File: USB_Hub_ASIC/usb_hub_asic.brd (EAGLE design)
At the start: 101.6 x 76.2 mm, 105 parts, among them J1 CONN_RCPT_USB3.0_TYPEB_9POS_R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, J2 CONN_RCPT_USB3.0_TYPEA_9POS_R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, J3 CONN_RCPT_USB3.0_TYPEA_9POS_R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, J4 CONN_RCPT_USB3.0_TYPEA_9POS_R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, J5 CONN_RCPT_USB3.0_TYPEA_9POS_R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, Q1 26M, U1 IC_MCP1603LT-330_3.3V_500MA_B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, U2 IC_CYUSB3314_QUAD_USB3.0_HUB, U3 IC_LM3674MF-1.2/NOPB_1.2V_600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

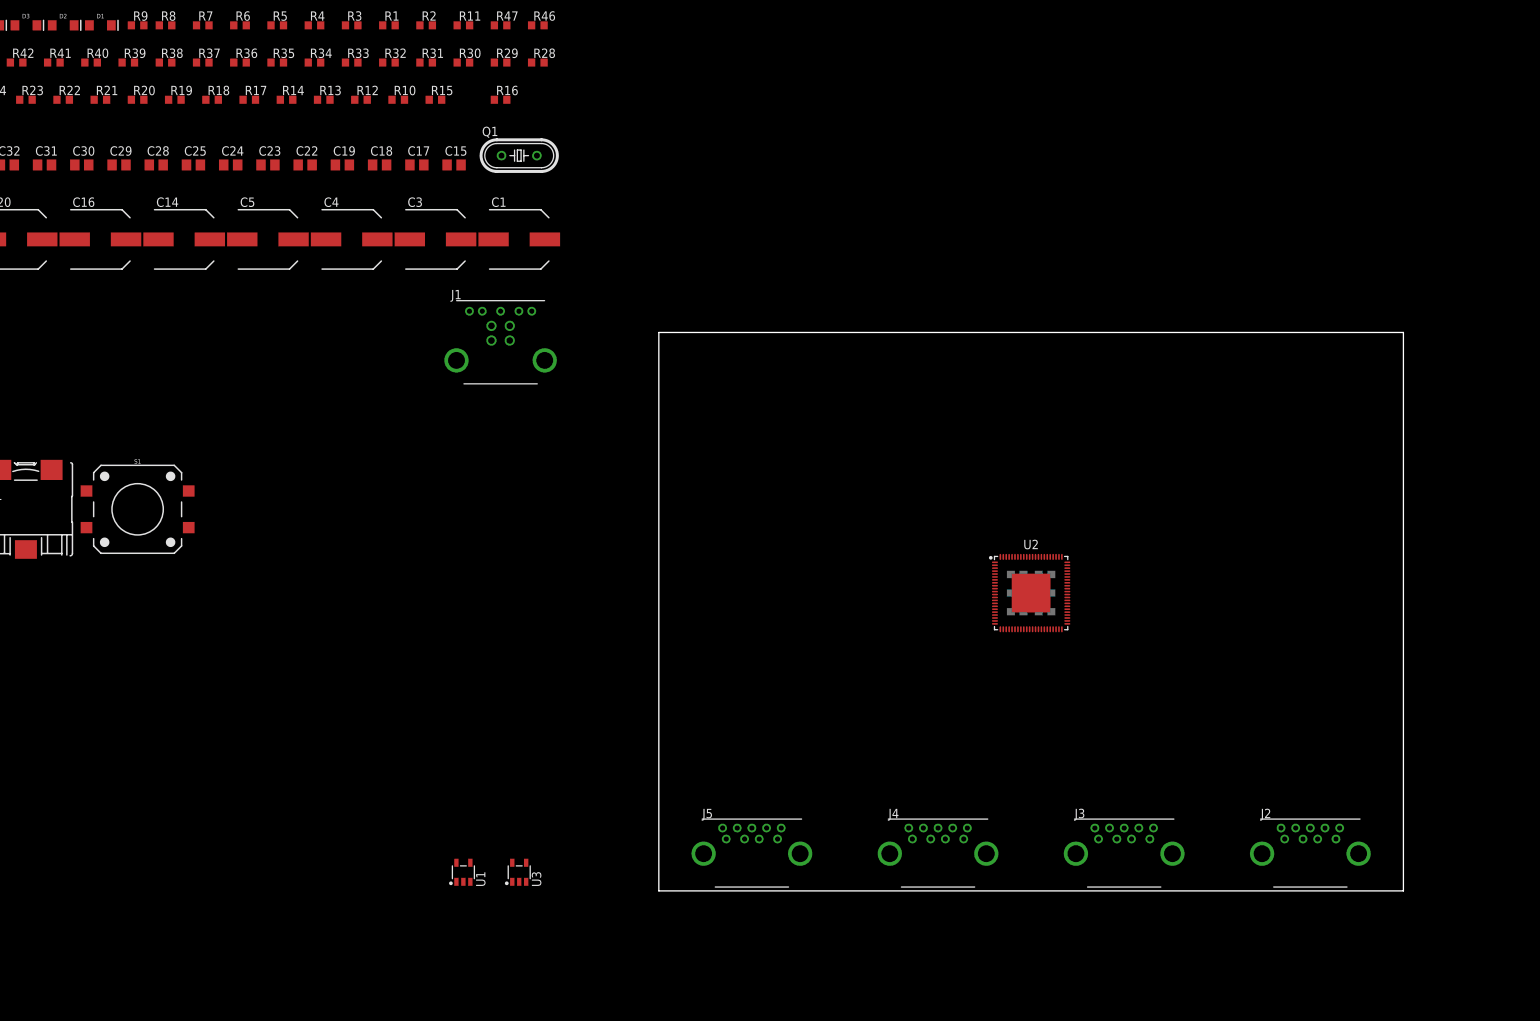
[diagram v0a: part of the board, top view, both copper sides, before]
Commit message: Power plane routing for chip
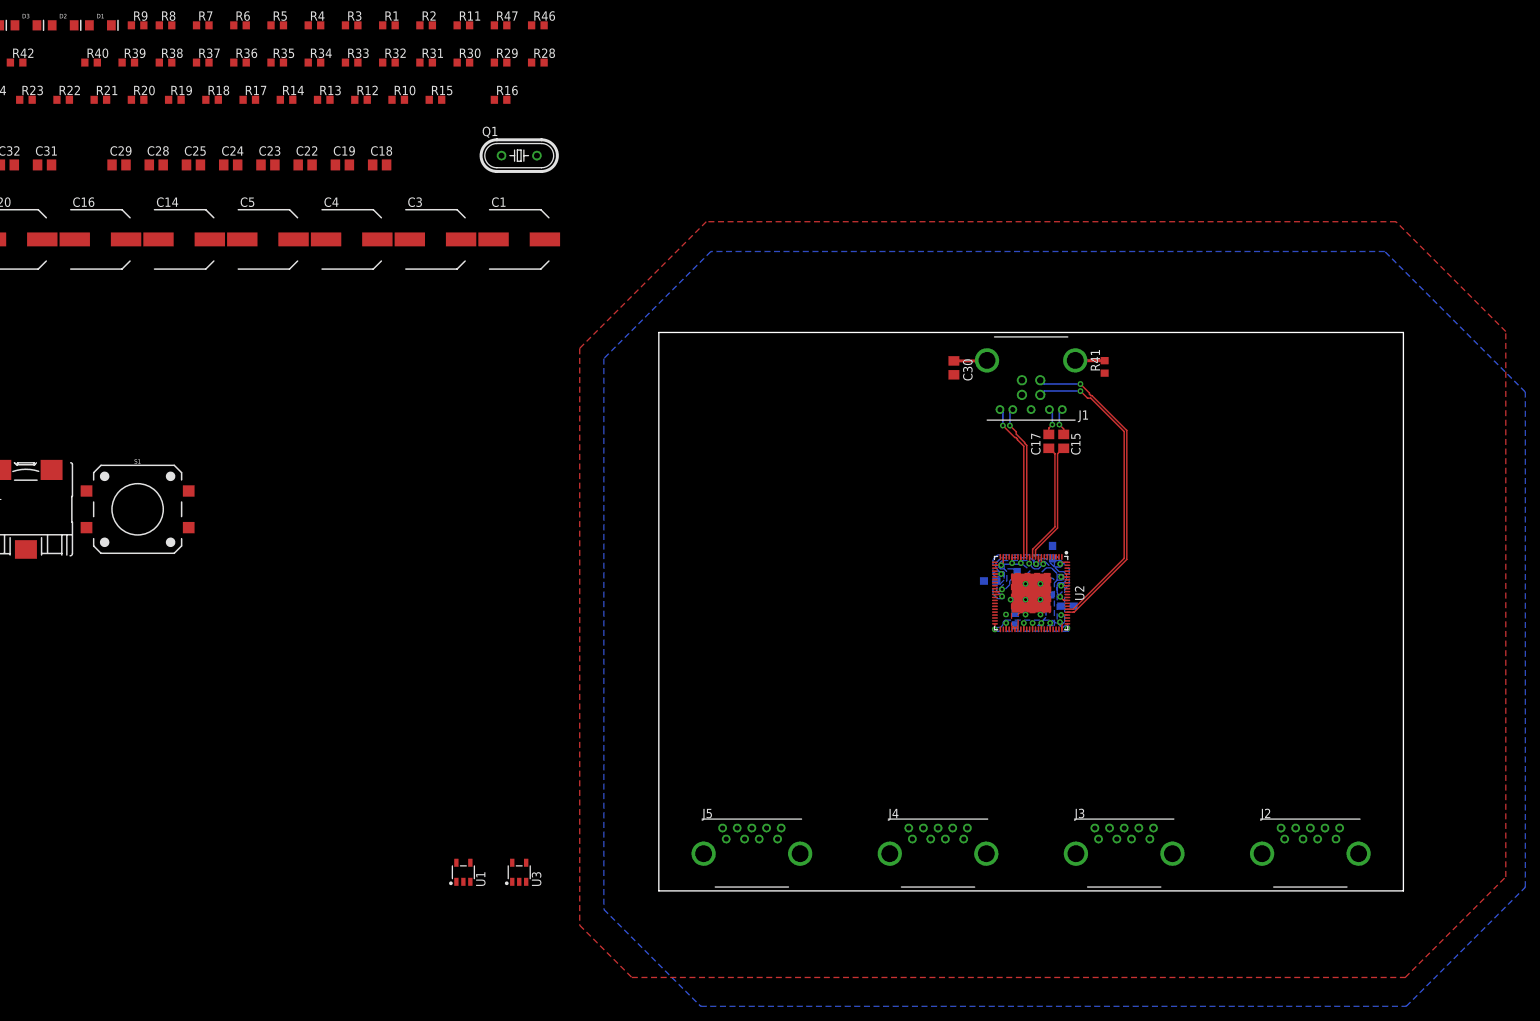
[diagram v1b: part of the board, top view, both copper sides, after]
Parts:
- moved R41 149.3 mm to (60.8, 71.5), turned to 90 degrees
- moved C30 122.2 mm to (40.3, 71.4), turned to 270 degrees
- moved C17 94.1 mm to (53.2, 61.3), turned to 90 degrees
- moved C15 91.3 mm to (55.2, 61.3), turned to 90 degrees
- moved J1 72.4 mm to (50.8, 72.4), turned to 180 degrees
- moved C7 8.19 mm to (53.7, 46.2), turned to 90 degrees
- moved C8 7.55 mm to (45.2, 42.3), turned to 0 degrees
- moved C6 7.08 mm to (55.8, 38.9)
- moved C9 5.40 mm to (48.6, 37.1), turned to 90 degrees
- moved C11 4.62 mm to (52.6, 40.4)
- moved C10 4.57 mm to (48.9, 42.7), turned to 270 degrees
- turned U2 to 270 degrees
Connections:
- net N$5 renamed US_N
- net N$6 renamed US_P
- net US_DM renamed US_D_N
- net US_DP renamed US_D_P
- net US_RXM renamed US_RX_N
- net US_RXP renamed US_RX_P
- net US_TXM renamed US_TX_N
- net US_TXP renamed US_TX_P
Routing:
- net US_D_P: track 0.00 -> 43.4 mm, vias 0 -> 1
- net US_D_N: track 0.00 -> 41.9 mm, vias 0 -> 1
- net US_RX_P: track 0.00 -> 21.5 mm, vias 0 -> 1
- net US_RX_N: track 0.00 -> 21.2 mm, vias 0 -> 1
- net US_TX_P: track 0.00 -> 16.5 mm
- net US_TX_N: track 0.00 -> 16.5 mm
- net +1V2: track 0.00 -> 13.4 mm, vias 0 -> 14
- net N$37: track 0.00 -> 8.58 mm
- net +3V3: track 0.00 -> 8.06 mm, vias 0 -> 8
- net US_N: track 0.00 -> 3.80 mm, vias 0 -> 1
- net US_P: track 0.00 -> 3.75 mm, vias 0 -> 1
- added copper zone on layer 16, net +1V2
- added copper zone on layer 16, net +3V3
- added copper zone on layer 1, net GND
- added copper zone on layer 16, net GND

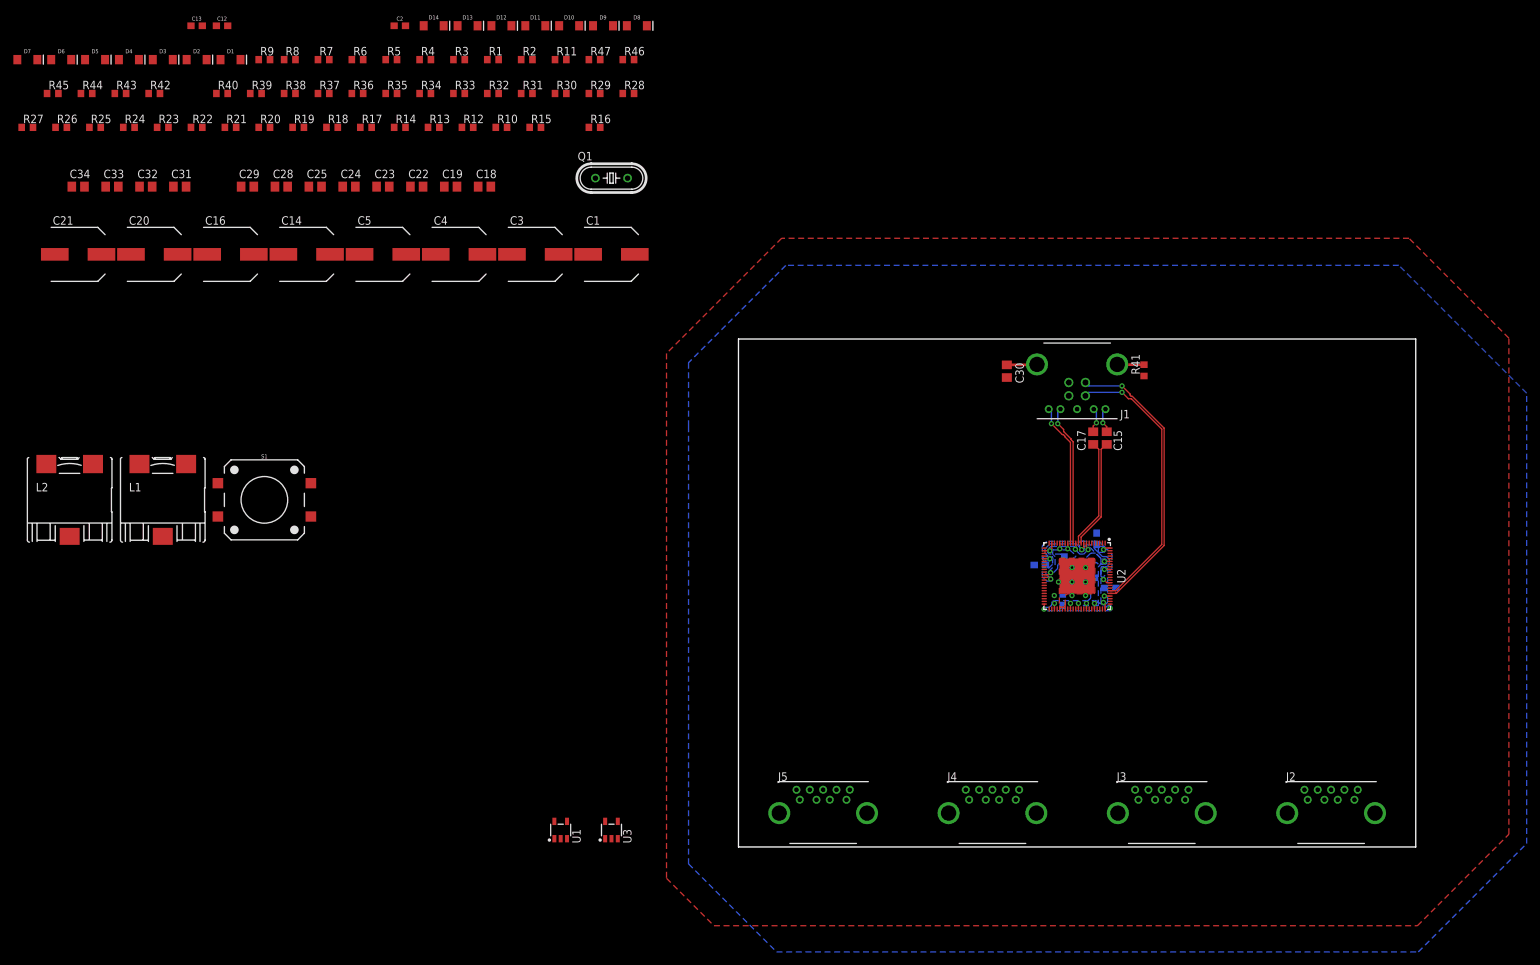
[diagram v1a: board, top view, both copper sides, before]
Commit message: Component selection and a bit more placement
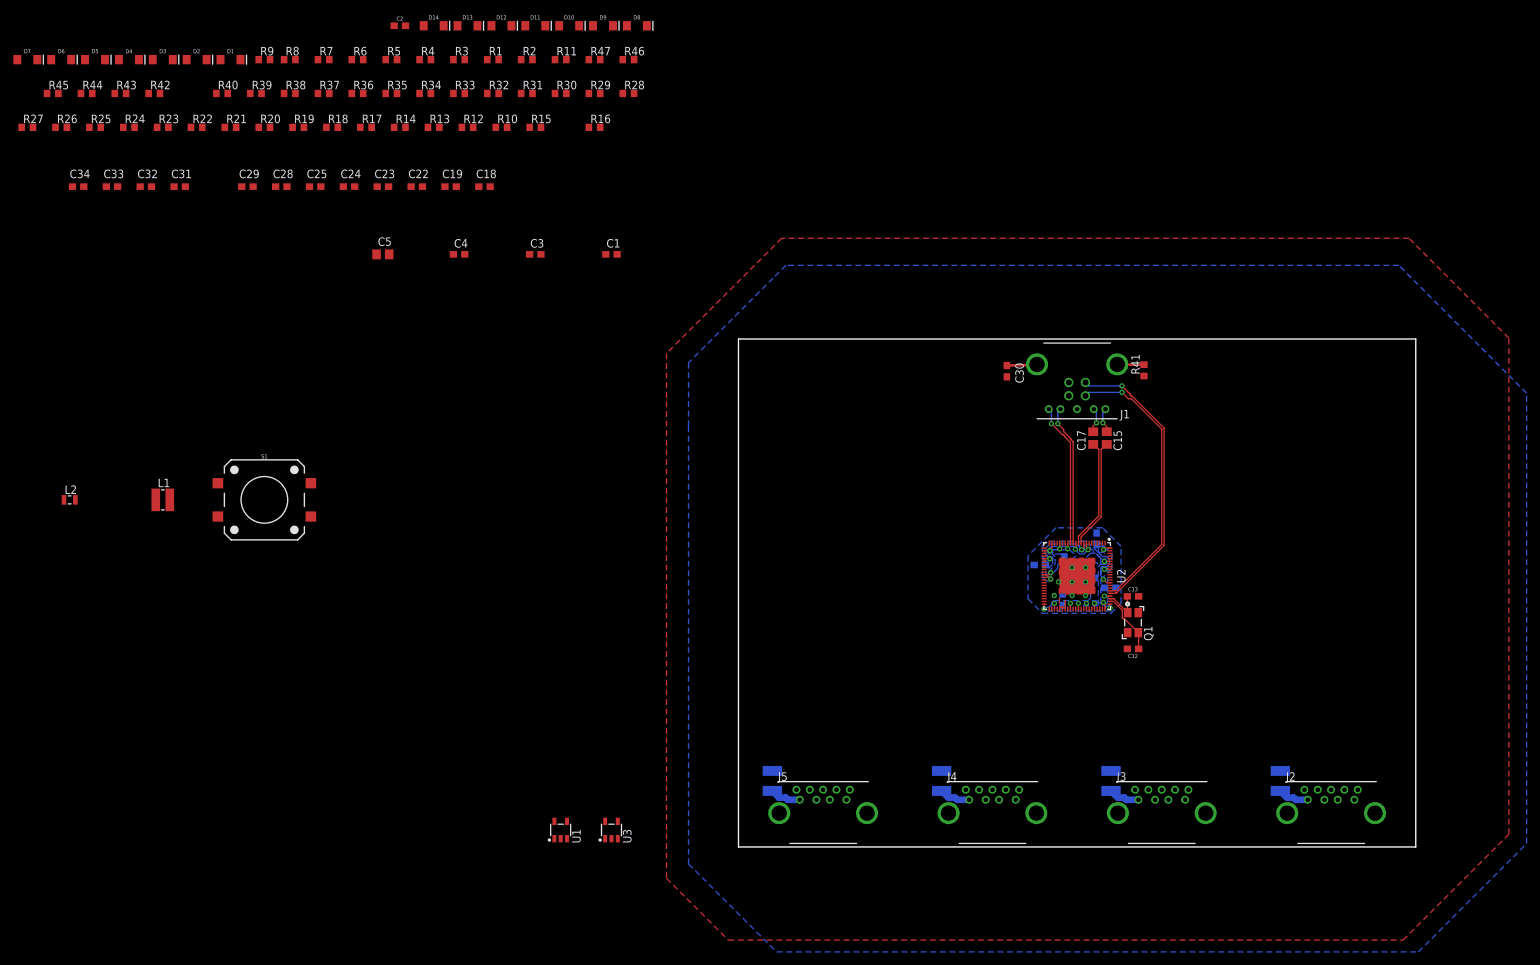
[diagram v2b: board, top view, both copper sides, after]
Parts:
- C1, C3, C4: device rcl:SANYO-OSCON_SMD_E12 -> rcl:C0603
- C10, C11, C12, C13, C6, C7, C8, C9: device SparkFun-Capacitors:0603 -> rcl:C0603
- C14, C16, C20, C21: device rcl:SANYO-OSCON_SMD_E12 -> rcl:C1210K
- C18, C19, C22, C23, C24, C25, C28, C29, C30, C31, C32, C33, C34: device rcl:C0805 -> rcl:C0603
- C5: device rcl:SANYO-OSCON_SMD_E12 -> rcl:C0805
- L1: device rcl:CEP125 -> USB_Hub_ASIC:SMD-1212(3030METRIC)
- L2: device rcl:CEP125 -> USB_Hub_ASIC:SMD-0805(2012METRIC)
- Q1: device crystal:HC49/S -> USB_Hub_ASIC:4-SMD-ECS-260-13-42-CKM-TR
- moved C20 186.5 mm to (81.3, 9.91), flipped to the bottom, turned to 90 degrees
- moved C12 165.6 mm to (59.2, 29.7), turned to 180 degrees
- moved C13 164.5 mm to (59.2, 37.6)
- moved C16 153.9 mm to (55.9, 9.91), flipped to the bottom, turned to 90 degrees
- moved C21 130.7 mm to (5.08, 9.91), flipped to the bottom, turned to 90 degrees
- moved C14 123.7 mm to (30.5, 9.91), flipped to the bottom, turned to 90 degrees
- moved Q1 102.8 mm to (59.2, 33.7), turned to 270 degrees
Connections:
- net DS1_DM renamed DS1_D_N
- net DS1_DP renamed DS1_D_P
- net DS1_RXM renamed DS1_RX_N
- net DS1_RXP renamed DS1_RX_P
- net DS1_TXM renamed DS1_TX_N
- net DS1_TXP renamed DS1_TX_P
- net DS2_DM renamed DS2_D_N
- net DS2_DP renamed DS2_D_P
- net DS2_RXM renamed DS2_RX_N
- net DS2_RXP renamed DS2_RX_P
- net DS2_TXM renamed DS2_TX_N
- net DS2_TXP renamed DS2_TX_P
- net DS3_DM renamed DS3_D_N
- net DS3_DP renamed DS3_D_P
- net DS3_RXM renamed DS3_RX_N
- net DS3_RXP renamed DS3_RX_P
- net DS3_TXM renamed DS3_TX_N
- net DS3_TXP renamed DS3_TX_P
- net DS4_DM renamed DS4_D_N
- net DS4_DP renamed DS4_D_P
- net DS4_RXM renamed DS4_RX_N
- net DS4_RXP renamed DS4_RX_P
- net DS4_TXM renamed DS4_TX_N
- net DS4_TXP renamed DS4_TX_P
- net N$1 renamed D1_N
- net N$10 renamed D2_P
- net N$13 renamed D3_N
- net N$14 renamed D3_P
- net N$17 renamed D4_N
- net N$18 renamed D4_P
- net N$2 renamed D1_P
- net N$9 renamed D2_N
- removed net N$3: C14.+, C16.+, C20.+, C21.+, J2.1, J3.1, J4.1, J5.1
- net +1V2: now also C5.1, L2.P$2; no longer C5.+, L2.2
- net +3V3: now also C3.1, L1.P$2; no longer C3.+, L1.2
- net +5V: now also C1.1, C14.1, C16.1, C20.1, C21.1, C4.1, J2.1, J3.1, J4.1, J5.1; no longer C1.+, C4.+
- net GND: now also C1.2, C14.2, C16.2, C20.2, C21.2, C3.2, C4.2, C5.2, Q1.P$2, Q1.P$4; no longer C1.-, C14.-, C16.-, C20.-, C21.-, C3.-, C4.-, C5.-
- net N$28: now also L2.P$1; no longer L2.1
- net N$30: now also L1.P$1; no longer L1.1
- net XTL_IN: now also Q1.P$1; no longer Q1.1
- net XTL_OUT: now also Q1.P$3; no longer Q1.2
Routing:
- net +5V: track 0.00 -> 18.7 mm
- net XTL_OUT: track 0.00 -> 9.32 mm
- net XTL_IN: track 0.00 -> 5.97 mm

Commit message: Board layout, need to place config resistors
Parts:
- removed J1: CONN_RCPT_USB3.0_TYPEB_9POS_R/A, USB_Hub_ASIC:CONN_RCPT_USB3.0_E8199-030-03
- removed J2, J3, J4, J5: CONN_RCPT_USB3.0_TYPEA_9POS_R/A, USB_Hub_ASIC:CONN_RCPT_USB3.0_UJ3-AH-4-TH
- removed S1: MOMENTARY-SWITCH-SPST-SMD-12MM, SparkFun-Switches:TACTILE_SWITCH_SMD_12MM
- added DS1, DS2, DS3, DS4: CONN_RCPT_USB3.0_TYPEA_9POS_R/A, USB_Hub_ASIC:CONN_RCPT_USB3.0_UJ3-AH-4-TH
- added SW1: RESET, USB_Hub_ASIC:SMD-TLSMDT3C020GLFS
- added US: CONN_RCPT_USB3.0_TYPEB_9POS_R/A, USB_Hub_ASIC:CONN_RCPT_USB3.0_E8199-030-03
- C15, C17: device rcl:C0805 -> rcl:C0603
- moved R22 263.6 mm to (156.2, -6.35)
- moved R26 261.5 mm to (151.1, 40.6)
- moved R8 251.4 mm to (151.1, -6.35)
- moved R38 246.5 mm to (151.1, -1.27)
- moved R7 244.2 mm to (156.2, 8.89)
- moved R6 238.6 mm to (153.7, 6.35)
- moved R34 233.1 mm to (156.2, -1.27)
- moved R4 233.1 mm to (156.2, 3.81)
- moved R5 233.1 mm to (151.1, 3.81)
- moved R3 227.8 mm to (153.7, 1.27)
- moved R33 227.8 mm to (153.7, -3.81)
- moved R42 207.2 mm to (91.4, 8.89), flipped to the bottom, turned to 270 degrees
- moved D4 200.8 mm to (73.7, 3.81), turned to 90 degrees
- moved R47 200.1 mm to (161.3, 36.8)
- moved C31 199.4 mm to (94.0, 8.89), flipped to the bottom, turned to 90 degrees
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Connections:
- net +5V: now also DS1.1, DS2.1, DS3.1, DS4.1, US.1; no longer J1.1, J2.1, J3.1, J4.1, J5.1
- net D1_N: now also DS1.8; no longer J2.8
- net D1_P: now also DS1.9; no longer J2.9
- net D2_N: now also DS2.8; no longer J4.8
- net D2_P: now also DS2.9; no longer J4.9
- net D3_N: now also DS3.8; no longer J3.8
- net D3_P: now also DS3.9; no longer J3.9
- net D4_N: now also DS4.8; no longer J5.8
- net D4_P: now also DS4.9; no longer J5.9
- net DS1_D_N: now also DS1.2; no longer J2.2
- net DS1_D_P: now also DS1.3; no longer J2.3
- net DS1_RX_N: now also DS1.5; no longer J2.5
- net DS1_RX_P: now also DS1.6; no longer J2.6
- net DS2_D_N: now also DS2.2; no longer J4.2
- net DS2_D_P: now also DS2.3; no longer J4.3
- net DS2_RX_N: now also DS2.5; no longer J4.5
- net DS2_RX_P: now also DS2.6; no longer J4.6
- net DS3_D_N: now also DS3.2; no longer J3.2
- net DS3_D_P: now also DS3.3; no longer J3.3
- net DS3_RX_N: now also DS3.5; no longer J3.5
- net DS3_RX_P: now also DS3.6; no longer J3.6
- net DS4_D_N: now also DS4.2; no longer J5.2
- net DS4_D_P: now also DS4.3; no longer J5.3
- net DS4_RX_N: now also DS4.5; no longer J5.5
- net DS4_RX_P: now also DS4.6; no longer J5.6
- net GND: now also DS1.4, DS1.7, DS2.4, DS2.7, DS3.4, DS3.7, DS4.4, DS4.7, SW1.A, US.4, US.7; no longer J1.4, J1.7, J2.4, J2.7, J3.4, J3.7, J4.4, J4.7, J5.4, J5.7, S1.3
- net N$37: now also US.SHIELD1, US.SHIELD2; no longer J1.SHIELD1, J1.SHIELD2
- net N$38: now also DS1.SHIELD1, DS1.SHIELD2; no longer J2.SHIELD1, J2.SHIELD2
- net N$39: now also DS2.SHIELD1, DS2.SHIELD2; no longer J4.SHIELD1, J4.SHIELD2
- net N$40: now also DS3.SHIELD1, DS3.SHIELD2; no longer J3.SHIELD1, J3.SHIELD2
- net N$41: now also DS4.SHIELD1, DS4.SHIELD2; no longer J5.SHIELD1, J5.SHIELD2
- net RESETIN: now also SW1.D; no longer S1.1
- net US_D_N: now also US.2; no longer J1.2
- net US_D_P: now also US.3; no longer J1.3
- net US_N: now also US.5; no longer J1.5
- net US_P: now also US.6; no longer J1.6
- net US_RX_N: now also US.8; no longer J1.8
- net US_RX_P: now also US.9; no longer J1.9
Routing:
- net US_D_P: track 43.4 -> 0.00 mm, vias 1 -> 0
- net US_D_N: track 41.9 -> 0.00 mm, vias 1 -> 0
- net US_RX_P: track 21.5 -> 0.00 mm, vias 1 -> 0
- net US_RX_N: track 21.2 -> 0.00 mm, vias 1 -> 0
- net US_TX_P: track 16.5 -> 0.00 mm
- net US_TX_N: track 16.5 -> 0.00 mm
- net N$30: track 0.00 -> 8.20 mm
- net D1_N: track 0.00 -> 5.88 mm, vias 0 -> 1
- net N$41: track 0.00 -> 5.60 mm
- net N$38: track 0.00 -> 5.60 mm
- net N$40: track 0.00 -> 5.60 mm
- net N$39: track 0.00 -> 5.60 mm
- net RESETIN: track 0.00 -> 5.58 mm
- net D4_N: track 0.00 -> 5.44 mm, vias 0 -> 1
- net D3_N: track 0.00 -> 5.44 mm, vias 0 -> 1
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- added copper zone on layer 16, net +5V
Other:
- board size 101.6 x 76.2 mm -> 96.5 x 50.8 mm

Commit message: more hectic routing
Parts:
- moved D9 82.6 mm to (6.35, 47.0)
- moved R18 82.6 mm to (6.35, 41.9)
- moved D10 82.5 mm to (2.54, 47.0)
- moved D8 82.5 mm to (10.2, 47.0)
- moved R17 82.5 mm to (10.2, 41.9)
- moved R19 82.5 mm to (2.54, 41.9)
- moved C17 78.7 mm to (88.9, 34.3)
- moved C15 78.7 mm to (91.4, 34.3)
- moved US 78.7 mm to (87.6, 47.0)
- moved R41 62.2 mm to (80.0, 43.2)
- moved C30 62.2 mm to (77.5, 43.2)
- moved D14 58.4 mm to (77.5, 45.7)
- moved R36 58.4 mm to (77.5, 40.6)
- moved C21 52.1 mm to (22.9, 47.0)
- moved C29 52.1 mm to (24.1, 36.8)
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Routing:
- net DS3_AMBER/VID_SEL[2]: track 0.00 -> 84.3 mm, vias 0 -> 4
- net DS2_AMBER/NON_REMOVABLE[0]: track 0.00 -> 80.7 mm, vias 0 -> 2
- net DS2_GREEN/NON_REMOVABLE[1]: track 0.00 -> 78.8 mm, vias 0 -> 2
- net DS4_LED_SS: track 0.00 -> 73.6 mm
- net DS3_LED_SS/PIN_STRAP: track 0.00 -> 72.8 mm, vias 0 -> 4
- net DS3_GREEN/VID_SEL[1]: track 0.00 -> 68.5 mm, vias 0 -> 6
- net DS4_AMBER/I2C_DEV_ID: track 0.00 -> 62.5 mm
- net +3V3: track 12.9 -> 71.9 mm, vias 8 -> 9
- net DS2_LED_SS/PWR_EN_SEL: track 0.00 -> 57.3 mm, vias 0 -> 4
- net DS3_D_P: track 0.00 -> 51.8 mm, vias 0 -> 1
- net DS3_D_N: track 0.00 -> 51.2 mm, vias 0 -> 1
- net DS4_GREEN/VID_SEL[0]: track 0.00 -> 50.9 mm
- net DS1_LED_SS/PORT_DISABLE[1]: track 0.00 -> 47.9 mm, vias 0 -> 2
- net DS1_D_P: track 0.00 -> 47.7 mm, vias 0 -> 1
- net DS4_D_P: track 0.00 -> 47.6 mm, vias 0 -> 1
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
